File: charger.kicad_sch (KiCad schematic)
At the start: 37 parts, among them Q1 NMOS, Q2 NMOS, U2 BQ25798RQMR

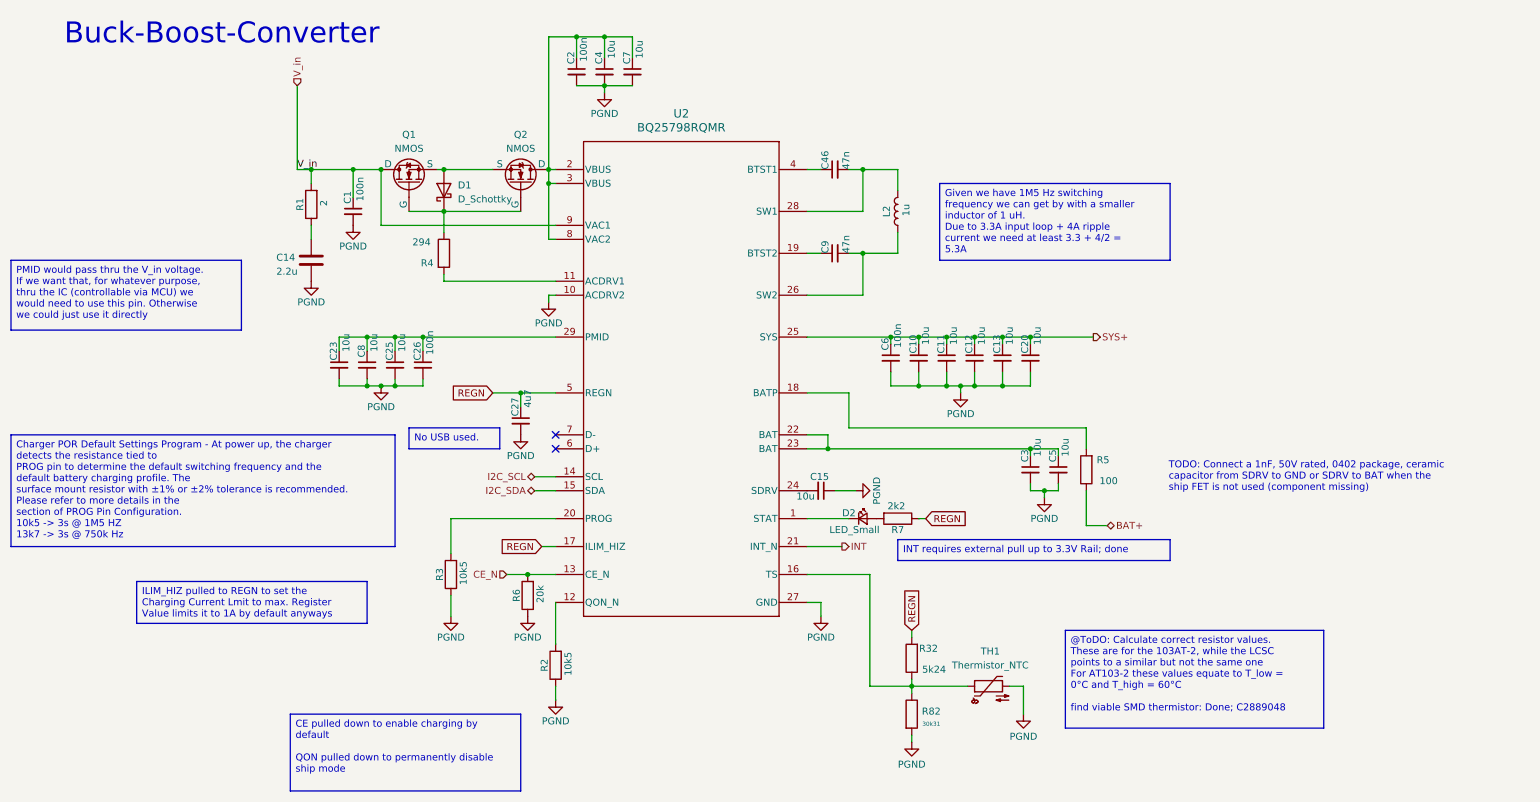
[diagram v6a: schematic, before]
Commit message: changed arming_pin2battery connection
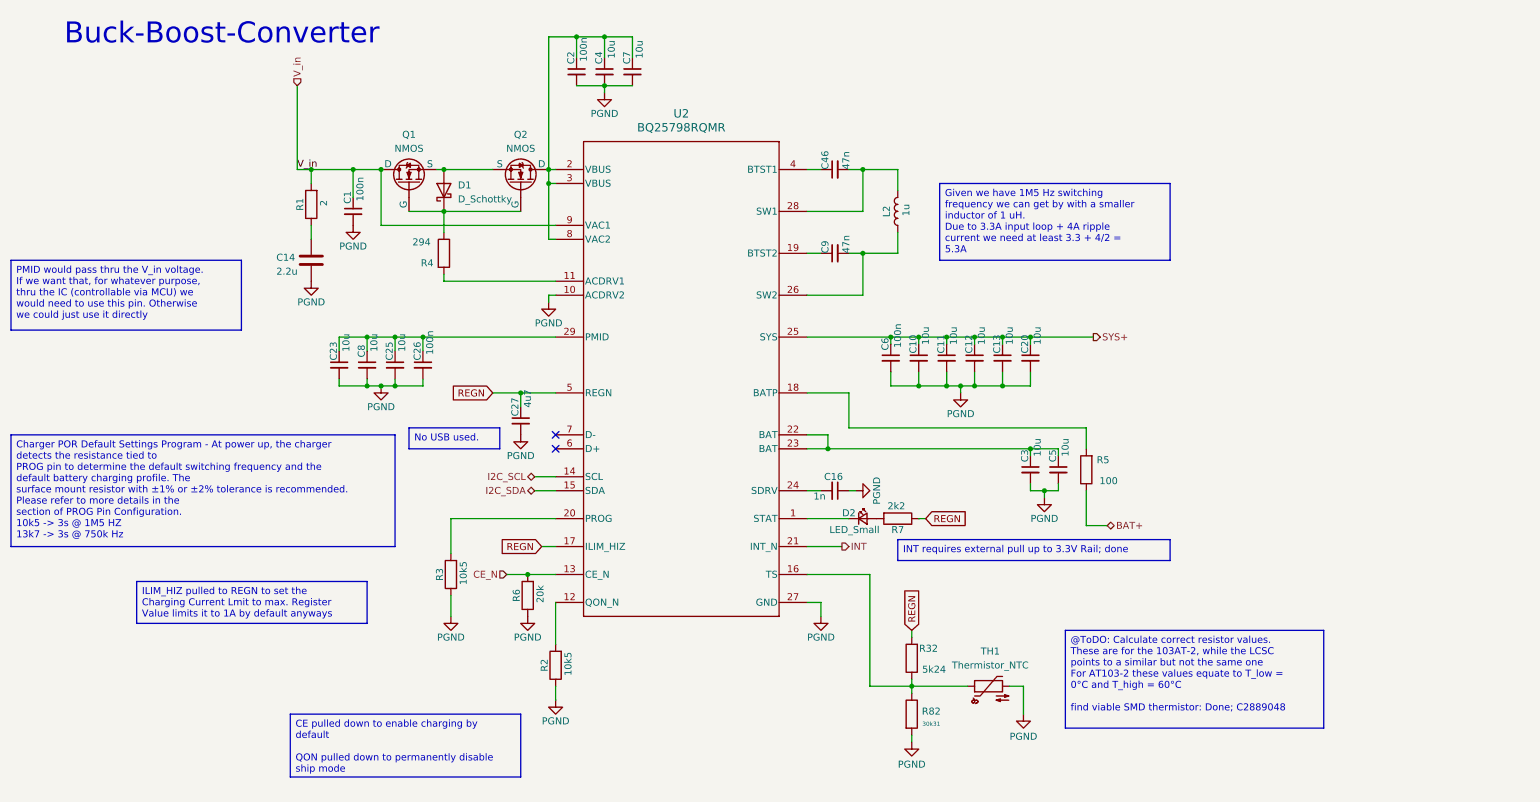
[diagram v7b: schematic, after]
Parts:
- removed C15: 10u, Capacitor_SMD:C_0402_1005Metric, symbol Device:C_Small
- added C16: 1n, Capacitor_SMD:C_0402_1005Metric, symbol Device:C_Small
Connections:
- net PGND: now also C16.1
- net at U2.24 (SDRV): now also C16.2
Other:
- note removed: "TODO: Connect a 1nF, 50V rated, 0402 package, ceramic capacitor from SDRV to GND or SDRV to BAT when the ship FET is not used (component missing)"
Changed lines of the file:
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@@
-		)
-	)
-	(text "TODO: Connect a 1nF, 50V rated, 0402 package, ceramic \ncapacitor from SDRV to GND or SDRV to BAT when the \nship FET is not used (component missing)"
-		(exclude_from_sim no)
-		(at 224.536 97.79 0)
-		(effects
-			(font
-				(size 1.27 1.27)
-			)
-			(justify left)
 		)
 	)
@@
 		(exclude_from_sim no)
 		(at 64.77 140.97 0)
-		(size 41.91 13.97)
+		(size 41.91 11.43)
 		(margins 0.9525 0.9525 0.9525 0.9525)
 		(stroke
@@
 	(wire
 		(pts
-			(xy 163.83 100.33) (xy 167.64 100.33)
+			(xy 166.37 100.33) (xy 167.64 100.33)
 		)
 		(stroke
@@
 		(pts
 			(xy 111.76 44.45) (xy 113.03 44.45)
+		)
+		(stroke
+			(width 0)
+			(type default)
+		)
+	)
+	(wire
+		(pts
+			(xy 161.29 100.33) (xy 158.75 100.33)
 		)
 		(stroke
@@
 	)
 	(symbol
+		(lib_id "Device:C_Small")
+		(at 163.83 100.33 270)
+		(mirror x)
+		(unit 1)
+		(exclude_from_sim no)
+		(in_bom yes)
+		(on_board yes)
+		(dnp no)
+		(property "Reference" "C16"
+			(at 163.576 97.79 90)
+			(effects
+				(font
+					(size 1.27 1.27)
+				)
+			)
+		)
+		(property "Value" "1n"
+			(at 161.036 101.346 90)
+			(effects
+				(font
+					(size 1.27 1.27)
+				)
+			)
+		)
+		(property "Footprint" "Capacitor_SMD:C_0402_1005Metric"
+			(at 163.83 100.33 0)
+			(effects
+				(font
+					(size 1.27 1.27)
+				)
+				(hide yes)
+			)
+		)
+		(property "Datasheet" "~"
+			(at 163.83 100.33 0)
+			(effects
+				(font
+					(size 1.27 1.27)
+				)
+				(hide yes)
+			)
+		)
+		(property "Description" "Unpolarized capacitor, small symbol"
+			(at 163.83 100.33 0)
+			(effects
+				(font
+					(size 1.27 1.27)
+				)
+				(hide yes)
+			)
+		)
+		(property "LCSC" "C1523"
+			(at 163.83 100.33 90)
+			(effects
+				(font
+					(size 1.27 1.27)
+				)
+				(hide yes)
+			)
+		)
+		(pin "2"
+		)
+		(pin "1"
+		)
+		(instances
+			(project "rapid_power_module"
+				(path "/afc8cbd3-9ea8-40a2-afae-ed6bd0fe7e6e/29a18ff5-2f4c-44c0-998a-9c2a7b324824"
+					(reference "C16")
+					(unit 1)
+				)
+			)
+		)
+	)
+	(symbol
 		(lib_id "power:GND1")
 		(at 177.8 146.05 0)
@@
 					(unit 1)
 				)
-			)
-		)
-	)
-	(symbol
-		(lib_id "Device:C_Small")
-		(at 161.29 100.33 270)
-		(mirror x)
-		(unit 1)
-		(exclude_from_sim no)
-		(in_bom yes)
-		(on_board yes)
-		(dnp no)
-		(property "Reference" "C15"
-			(at 161.036 97.79 90)
-			(effects
-				(font
-					(size 1.27 1.27)
-				)
-			)
-		)
-		(property "Value" "10u"
-			(at 158.496 101.346 90)
-			(effects
-				(font
-					(size 1.27 1.27)
-				)
-			)
-		)
-		(property "Footprint" "Capacitor_SMD:C_0402_1005Metric"
-			(at 161.29 100.33 0)
-			(effects
-				(font
-					(size 1.27 1.27)
-				)
-				(hide yes)
-			)
-		)
-		(property "Datasheet" "~"
-			(at 161.29 100.33 0)
-			(effects
-				(font
-					(size 1.27 1.27)
-				)
-				(hide yes)
-			)
-		)
-		(property "Description" "Unpolarized capacitor, small symbol"
-			(at 161.29 100.33 0)
-			(effects
-				(font
-					(size 1.27 1.27)
-				)
-				(hide yes)
-			)
-		)
-		(property "LCSC" "C307331"
-			(at 161.29 100.33 90)
-			(effects
-				(font
-					(size 1.27 1.27)
-				)
-				(hide yes)
-			)
-		)
-		(pin "2"
-		)
-		(pin "1"
-		)
-		(instances
-			(project "rapid_power_module"
-				(path "/afc8cbd3-9ea8-40a2-afae-ed6bd0fe7e6e/29a18ff5-2f4c-44c0-998a-9c2a7b324824"
-					(reference "C15")
-					(unit 1)
-				)

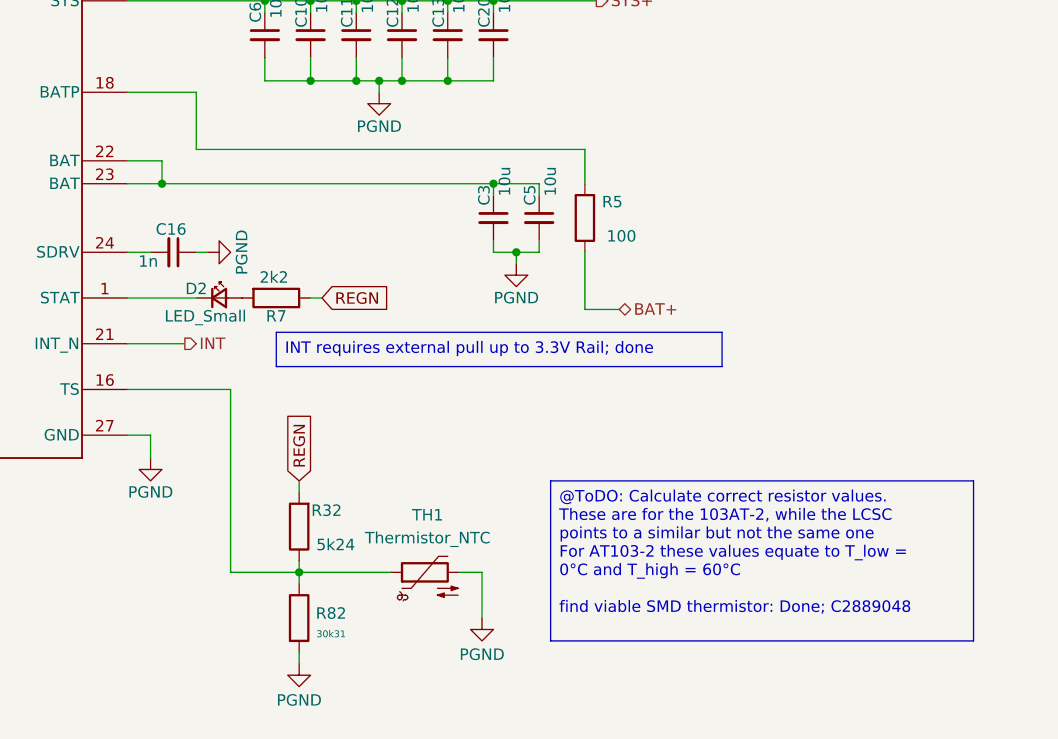
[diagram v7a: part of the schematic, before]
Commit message: implemented changes according to errors found in the schematic design review (wip)
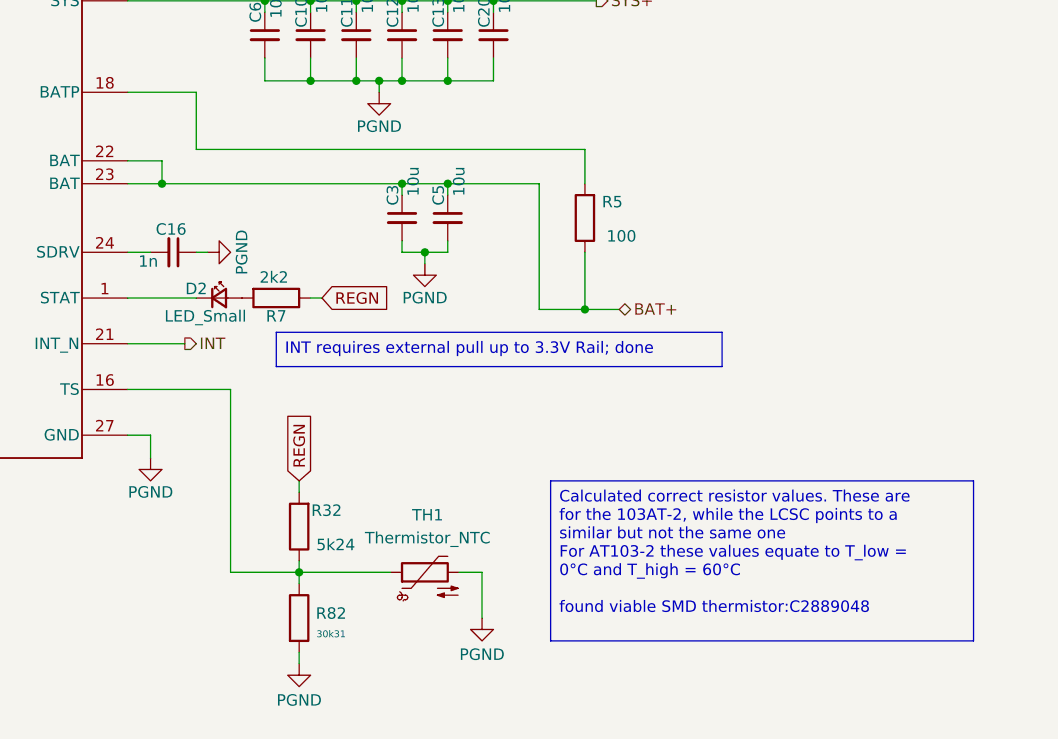
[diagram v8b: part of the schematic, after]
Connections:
- net BAT+: now also C3.1, C5.1, U2.22 (BAT), U2.23 (BAT)
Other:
- moved on the sheet: C3, C5
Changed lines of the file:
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@@
 		)
 	)
-	(text_box "@ToDO: Calculate correct resistor values. These are for the 103AT-2, while the LCSC points to a similar but not the same one\nFor AT103-2 these values equate to T_low = 0°C and T_high = 60°C\n\nfind viable SMD thermistor: Done; C2889048"
+	(text_box "Calculated correct resistor values. These are for the 103AT-2, while the LCSC points to a similar but not the same one\nFor AT103-2 these values equate to T_low = 0°C and T_high = 60°C\n\nfound viable SMD thermistor:C2889048"
 		(exclude_from_sim no)
 		(at 205.74 125.73 0)
@@
 	)
 	(junction
+		(at 194.31 92.71)
+		(diameter 0)
+		(color 0 0 0 0)
+	)
+	(junction
 		(at 179.07 72.39)
 		(diameter 0)
@@
 	)
 	(junction
+		(at 189.23 92.71)
+		(diameter 0)
+		(color 0 0 0 0)
+	)
+	(junction
 		(at 83.82 81.28)
 		(diameter 0)
@@
 	)
 	(junction
+		(at 209.55 106.68)
+		(diameter 0)
+		(color 0 0 0 0)
+	)
+	(junction
 		(at 194.31 81.28)
 		(diameter 0)
@@
 	)
 	(junction
-		(at 199.39 92.71)
-		(diameter 0)
-		(color 0 0 0 0)
-	)
-	(junction
 		(at 78.74 81.28)
 		(diameter 0)
@@
 	)
 	(junction
-		(at 201.93 100.33)
+		(at 191.77 100.33)
 		(diameter 0)
 		(color 0 0 0 0)
@@
 	(wire
 		(pts
+			(xy 194.31 92.71) (xy 204.47 92.71)
+		)
+		(stroke
+			(width 0)
+			(type default)
+		)
+	)
+	(wire
+		(pts
 			(xy 184.15 78.74) (xy 184.15 81.28)
 		)
@@
 	(wire
 		(pts
-			(xy 204.47 100.33) (xy 201.93 100.33)
+			(xy 194.31 100.33) (xy 191.77 100.33)
 		)
 		(stroke
@@
 	(wire
 		(pts
-			(xy 162.56 92.71) (xy 199.39 92.71)
+			(xy 162.56 92.71) (xy 189.23 92.71)
 		)
 		(stroke
@@
 	(wire
 		(pts
+			(xy 189.23 92.71) (xy 194.31 92.71)
+		)
+		(stroke
+			(width 0)
+			(type default)
+		)
+	)
+	(wire
+		(pts
 			(xy 113.03 135.89) (xy 113.03 138.43)
 		)
@@
 	(wire
 		(pts
-			(xy 199.39 92.71) (xy 204.47 92.71)
-		)
-		(stroke
-			(width 0)
-			(type default)
-		)
-	)
-	(wire
-		(pts
 			(xy 199.39 73.66) (xy 199.39 72.39)
 		)
@@
 	(wire
 		(pts
-			(xy 199.39 92.71) (xy 199.39 93.98)
+			(xy 189.23 92.71) (xy 189.23 93.98)
 		)
 		(stroke
@@
 	(wire
 		(pts
-			(xy 204.47 93.98) (xy 204.47 92.71)
+			(xy 194.31 93.98) (xy 194.31 92.71)
 		)
 		(stroke
@@
 	(wire
 		(pts
+			(xy 204.47 106.68) (xy 209.55 106.68)
+		)
+		(stroke
+			(width 0)
+			(type default)
+		)
+	)
+	(wire
+		(pts
 			(xy 86.36 49.53) (xy 92.71 49.53)
 		)
@@
 	(wire
 		(pts
-			(xy 199.39 99.06) (xy 199.39 100.33)
+			(xy 189.23 99.06) (xy 189.23 100.33)
 		)
 		(stroke
@@
 	(wire
 		(pts
-			(xy 204.47 99.06) (xy 204.47 100.33)
+			(xy 194.31 99.06) (xy 194.31 100.33)
 		)
 		(stroke
@@
 	(wire
 		(pts
-			(xy 201.93 101.6) (xy 201.93 100.33)
+			(xy 191.77 101.6) (xy 191.77 100.33)
 		)
 		(stroke
@@
 	(wire
 		(pts
+			(xy 204.47 92.71) (xy 204.47 106.68)
+		)
+		(stroke
+			(width 0)
+			(type default)
+		)
+	)
+	(wire
+		(pts
 			(xy 170.18 135.89) (xy 177.8 135.89)
 		)
@@
 	(wire
 		(pts
-			(xy 201.93 100.33) (xy 199.39 100.33)
+			(xy 191.77 100.33) (xy 189.23 100.33)
 		)
 		(stroke
@@
 	(symbol
 		(lib_id "Device:C_Small")
-		(at 204.47 96.52 0)
+		(at 194.31 96.52 0)
 		(mirror y)
 		(unit 1)
@@
 		(dnp no)
 		(property "Reference" "C5"
-			(at 203.454 93.98 90)
+			(at 193.294 93.98 90)
 			(effects
 				(font
@@
 		)
 		(property "Value" "10u"
-			(at 205.74 92.456 90)
+			(at 195.58 92.456 90)
 			(effects
 				(font
@@
 		)
 		(property "Footprint" "Capacitor_SMD:C_0402_1005Metric"
-			(at 204.47 96.52 0)
+			(at 194.31 96.52 0)
 			(effects
 				(font
@@
 		)
 		(property "Datasheet" "~"
-			(at 204.47 96.52 0)
+			(at 194.31 96.52 0)
 			(effects
 				(font
@@
 		)
 		(property "Description" "Unpolarized capacitor, small symbol"
-			(at 204.47 96.52 0)
+			(at 194.31 96.52 0)
 			(effects
 				(font
@@
 		)
 		(property "LCSC" "C307331"
-			(at 204.47 96.52 90)
+			(at 194.31 96.52 90)
 			(effects
 				(font
@@
 	(symbol
 		(lib_id "power:GND1")
-		(at 201.93 101.6 0)
+		(at 191.77 101.6 0)
 		(unit 1)
 		(exclude_from_sim no)
@@
 		(dnp no)
 		(property "Reference" "#PWR011"
-			(at 201.93 107.95 0)
+			(at 191.77 107.95 0)
 			(effects
 				(font
@@
 		)
 		(property "Value" "PGND"
-			(at 201.93 105.41 0)
+			(at 191.77 105.41 0)
 			(effects
 				(font
@@
 		)
 		(property "Footprint" ""
-			(at 201.93 101.6 0)
+			(at 191.77 101.6 0)
 			(effects
 				(font
@@
 		)
 		(property "Datasheet" ""
-			(at 201.93 101.6 0)
+			(at 191.77 101.6 0)
 			(effects
 				(font
@@
 		)
 		(property "Description" "Power symbol creates a global label with name \"GND1\" , ground"
-			(at 201.93 101.6 0)
+			(at 191.77 101.6 0)
 			(effects
 				(font
@@
 	(symbol
 		(lib_id "Device:C_Small")
-		(at 199.39 96.52 0)
+		(at 189.23 96.52 0)
 		(mirror y)
 		(unit 1)
@@
 		(dnp no)
 		(property "Reference" "C3"
-			(at 198.374 93.98 90)
+			(at 188.214 93.98 90)
 			(effects
 				(font
@@
 		)
 		(property "Value" "10u"
-			(at 200.66 92.456 90)
+			(at 190.5 92.456 90)
 			(effects
 				(font
@@
 		)
 		(property "Footprint" "Capacitor_SMD:C_0402_1005Metric"
-			(at 199.39 96.52 0)
+			(at 189.23 96.52 0)
 			(effects
 				(font
@@
 		)
 		(property "Datasheet" "~"
-			(at 199.39 96.52 0)
+			(at 189.23 96.52 0)
 			(effects
 				(font
@@
 		)
 		(property "Description" "Unpolarized capacitor, small symbol"
-			(at 199.39 96.52 0)
+			(at 189.23 96.52 0)
 			(effects
 				(font
@@
 		)
 		(property "LCSC" "C307331"
-			(at 199.39 96.52 90)
+			(at 189.23 96.52 90)
 			(effects
 				(font
